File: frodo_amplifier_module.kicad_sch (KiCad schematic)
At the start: 37 parts, among them IC1 INA826AID, U1 ADC101C021CIMK, U2 MCP6001-OT, U3 MIC5504-3.3YM5, U4 REF3033

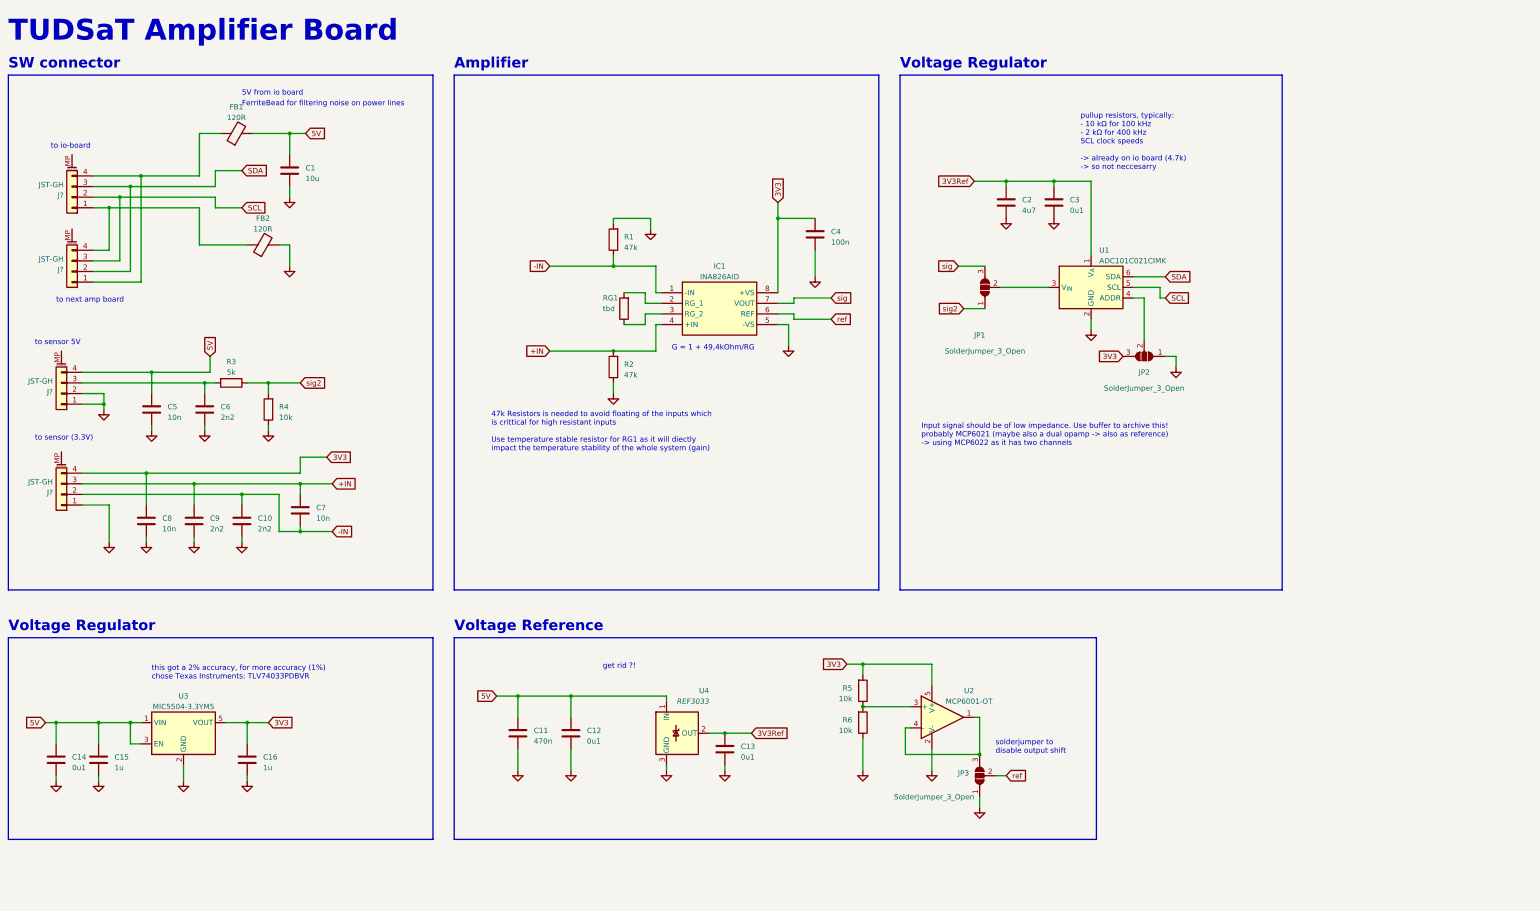
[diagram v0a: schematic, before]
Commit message: remove 3v3ref, merge fills, adjust layout, fill BOM
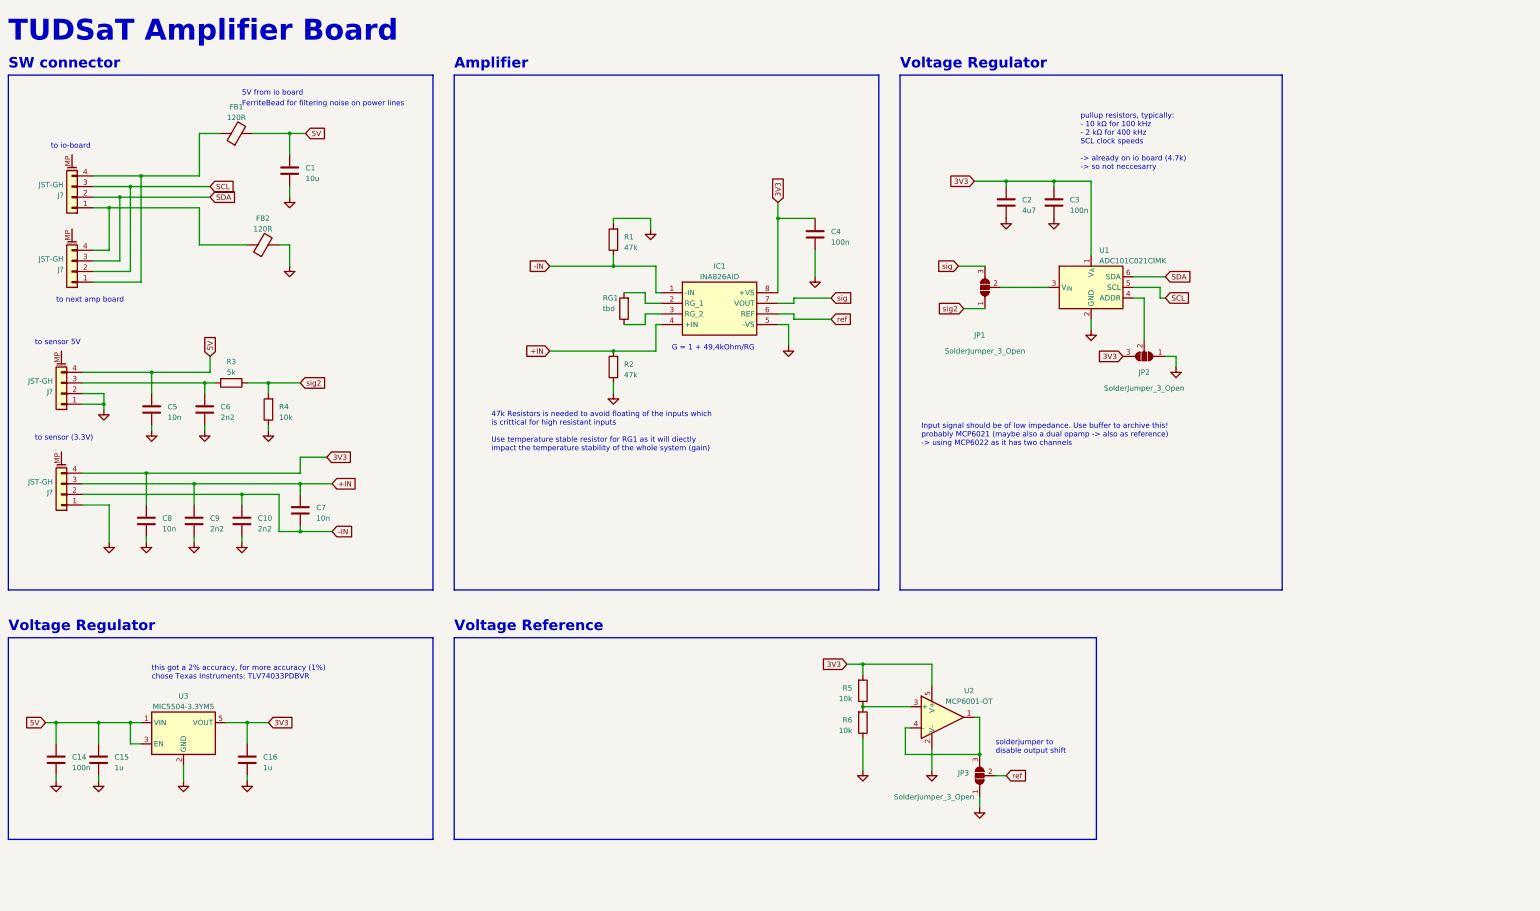
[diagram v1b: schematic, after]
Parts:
- removed C11: 470n, Capacitor_SMD:C_0402_1005Metric, symbol Device:C
- removed C12, C13: 0u1, Capacitor_SMD:C_0402_1005Metric, symbol Device:C
- removed U4: REF3033, Package_TO_SOT_SMD:SOT-23, symbol Reference_Voltage:REF3033
- C1: LCSC (none) -> C315248
- C10, C6, C9: LCSC (none) -> C84703
- C14, C3: value 0u1 -> 100n; LCSC (none) -> C1525
- C15, C16: LCSC (none) -> C76999
- C2: LCSC (none) -> C23733
- C4: LCSC (none) -> C1525
- C5, C7, C8: LCSC (none) -> C15195
- FB1, FB2: LCSC (none) -> C76891
- IC1: LCSC (none) -> C38433
- J? (x4): LCSC (none) -> C161692; LCSC# C161692 -> (none)
- R1, R2: LCSC (none) -> C25792
- R3: LCSC (none) -> C477765
- R4, R5, R6: LCSC (none) -> C25744
- U1: LCSC (none) -> C701589
- U2: LCSC (none) -> C116490
- U3: LCSC (none) -> C3021093
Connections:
- net 3V3Ref is gone; now on net 3V3: C2.1, C3.1, U1.1 (V_{A})
- net SCL: now also J?.2 (Pin_2), J?.3 (Pin_3); no longer J?.2 (Pin_2), J?.3 (Pin_3)
- net SDA: now also J?.2 (Pin_2), J?.3 (Pin_3); no longer J?.2 (Pin_2), J?.3 (Pin_3)
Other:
- note removed: "get rid ?!"

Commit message: finished amp module rev3
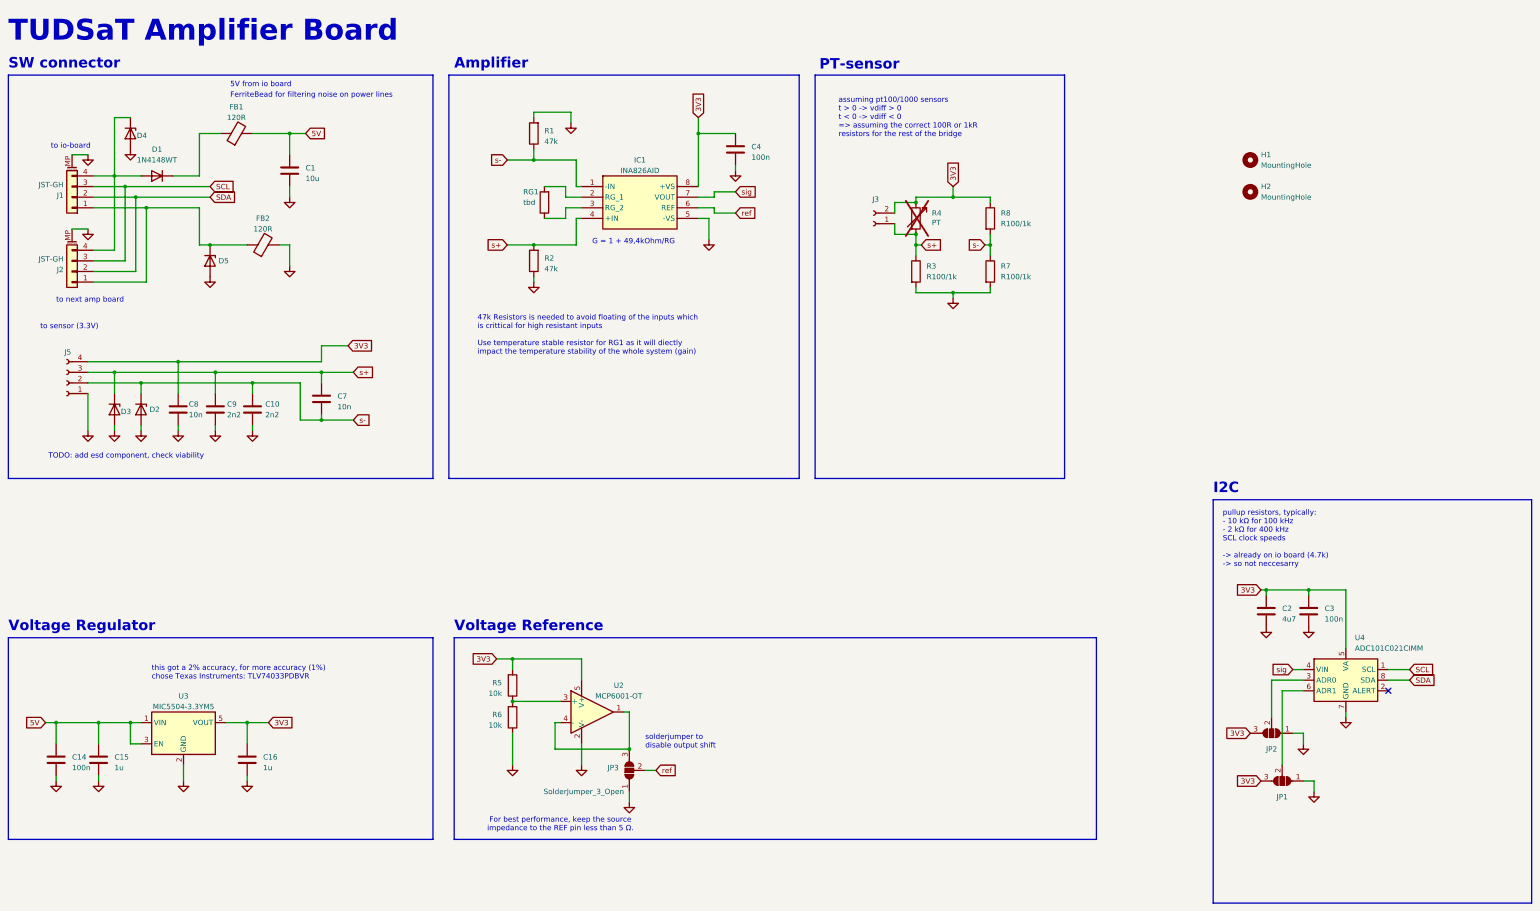
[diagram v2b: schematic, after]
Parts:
- removed C5: 10n, Capacitor_SMD:C_0402_1005Metric, symbol Device:C
- removed C6: 2n2, Capacitor_SMD:C_0402_1005Metric, symbol Device:C
- removed J? (x2): JST-GH, Connector_JST:JST_GH_SM04B-GHS-TB_1x04-1MP_P1.25mm_Horizontal, symbol Connector_Generic_MountingPin:Conn_01x04_MountingPin
- removed R4: 10k, Resistor_SMD:R_0402_1005Metric_Pad0.72x0.64mm_HandSolder, symbol Device:R
- removed U1: ADC101C021CIMK, Package_TO_SOT_SMD:SOT-23-6, symbol Analog_ADC:ADC101C021CIMK
- added D1: 1N4148WT, Diode_SMD:D_SOD-523, symbol Diode:1N4148WT
- added D2, D3, D4, D5: ESD5Zxx, Diode_SMD:D_SOD-523, symbol Diode:ESD5Zxx
- added H1, H2: MountingHole, MountingHole:MountingHole_2.2mm_M2_DIN965_Pad, symbol Mechanical:MountingHole
- added J3: Conn_01x02_Socket, Resistor_THT:R_Axial_DIN0204_L3.6mm_D1.6mm_P1.90mm_Vertical, symbol Connector:Conn_01x02_Socket
- added J5: Conn_01x04_Socket, Connector_PinHeader_1.27mm:PinHeader_1x04_P1.27mm_Vertical, symbol Connector:Conn_01x04_Socket
- added R4: PT, symbol Device:R_Variable
- added R7, R8: R100/1k, Resistor_SMD:R_0805_2012Metric_Pad1.20x1.40mm_HandSolder, symbol Device:R
- added U4: ADC101C021CIMM, Package_SO:MSOP-8_3x3mm_P0.65mm, symbol Analog_ADC:ADC101C021CIMM
- JP1: value SolderJumper_3_Open -> ADR1
- JP2: value SolderJumper_3_Open -> ADR0
- JP3: footprint Jumper:SolderJumper-3_P1.3mm_Open_RoundedPad1.0x1.5mm_NumberLabels -> Jumper:SolderJumper-3_P1.3mm_Open_Pad1.0x1.5mm
- R3: value 5k -> R100/1k; footprint Resistor_SMD:R_0402_1005Metric_Pad0.72x0.64mm_HandSolder -> Resistor_SMD:R_0805_2012Metric_Pad1.20x1.40mm_HandSolder; LCSC C477765 -> (none)
- RG1: footprint Resistor_SMD:R_0603_1608Metric -> Resistor_SMD:R_1206_3216Metric_Pad1.30x1.75mm_HandSolder
- gave numbers to parts that had none: 2
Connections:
- net 3V3: now also JP1.3 (B), J3.2 (Pin_2), J5.4 (Pin_4), R4.1, R8.1, U4.5 (VA)
- net GND: now also J1.MP (MountPin), J2.MP (MountPin), JP1.1 (A), R3.2, D2.2 (A), D3.2 (A), D4.2 (A), D5.2 (A), J5.1 (Pin_1), R7.2, U4.7 (GND)
- net SCL: now also J2.3 (Pin_3), U4.1 (SCL); no longer J2.2 (Pin_2)
- net SDA: now also J2.2 (Pin_2), U4.8 (SDA); no longer J2.3 (Pin_3)
- net sig: now also U4.4 (VIN); no longer JP1.3 (B)
- net at FB2.1, J1.1 (Pin_1): now also J2.1 (Pin_1), D5.1 (K); no longer J2.4 (Pin_4)
- net at JP2.2 (C): now also U4.3 (ADR0)
- net at JP1.2 (C): now also U4.6 (ADR1)
- net +IN renamed s+
- net s+: now also R3.1, D3.1 (K), J3.1 (Pin_1), J5.3 (Pin_3), R4.2
- net -IN renamed s-
- net s-: now also D2.1 (K), J5.2 (Pin_2), R7.1, R8.2
- removed net sig2: JP1.1 (A), R3.1
- new net: D1.2 (A), D4.1 (K), J1.4 (Pin_4), J2.4 (Pin_4)
- new net: D1.1 (K), FB1.1
- no-connect marks 0 -> 1
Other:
- note added: "For best performance, keep the source impedance to the REF pin less than 5 Ω."
- note added: "I2C"
- note added: "PT-sensor"
- note added: "TODO: add esd component, check viability"
- note added: "assuming pt100/1000 sensors t > 0 -> vdiff > 0 t < 0 -> vdiff < 0 => assuming the correct 100R or 1kR resistors for the rest of the bridge"
- note removed: "Input signal should be of low impedance. Use buffer to archive this! probably MCP6021 (maybe also a dual opamp -> also as reference) -> using MCP6022 as it has two channels"
- note removed: "to sensor 5V"
- moved on the sheet: C10, C2, C3, C4, C7, C8, C9, IC1, JP2, JP3, R1, R2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
